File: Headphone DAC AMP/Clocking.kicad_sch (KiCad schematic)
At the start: 13 parts, among them Y1 Crystal_GND24, Y2 LMK6CE049152CDLFR, Y3 ASDLJ-E-45.1584MHz

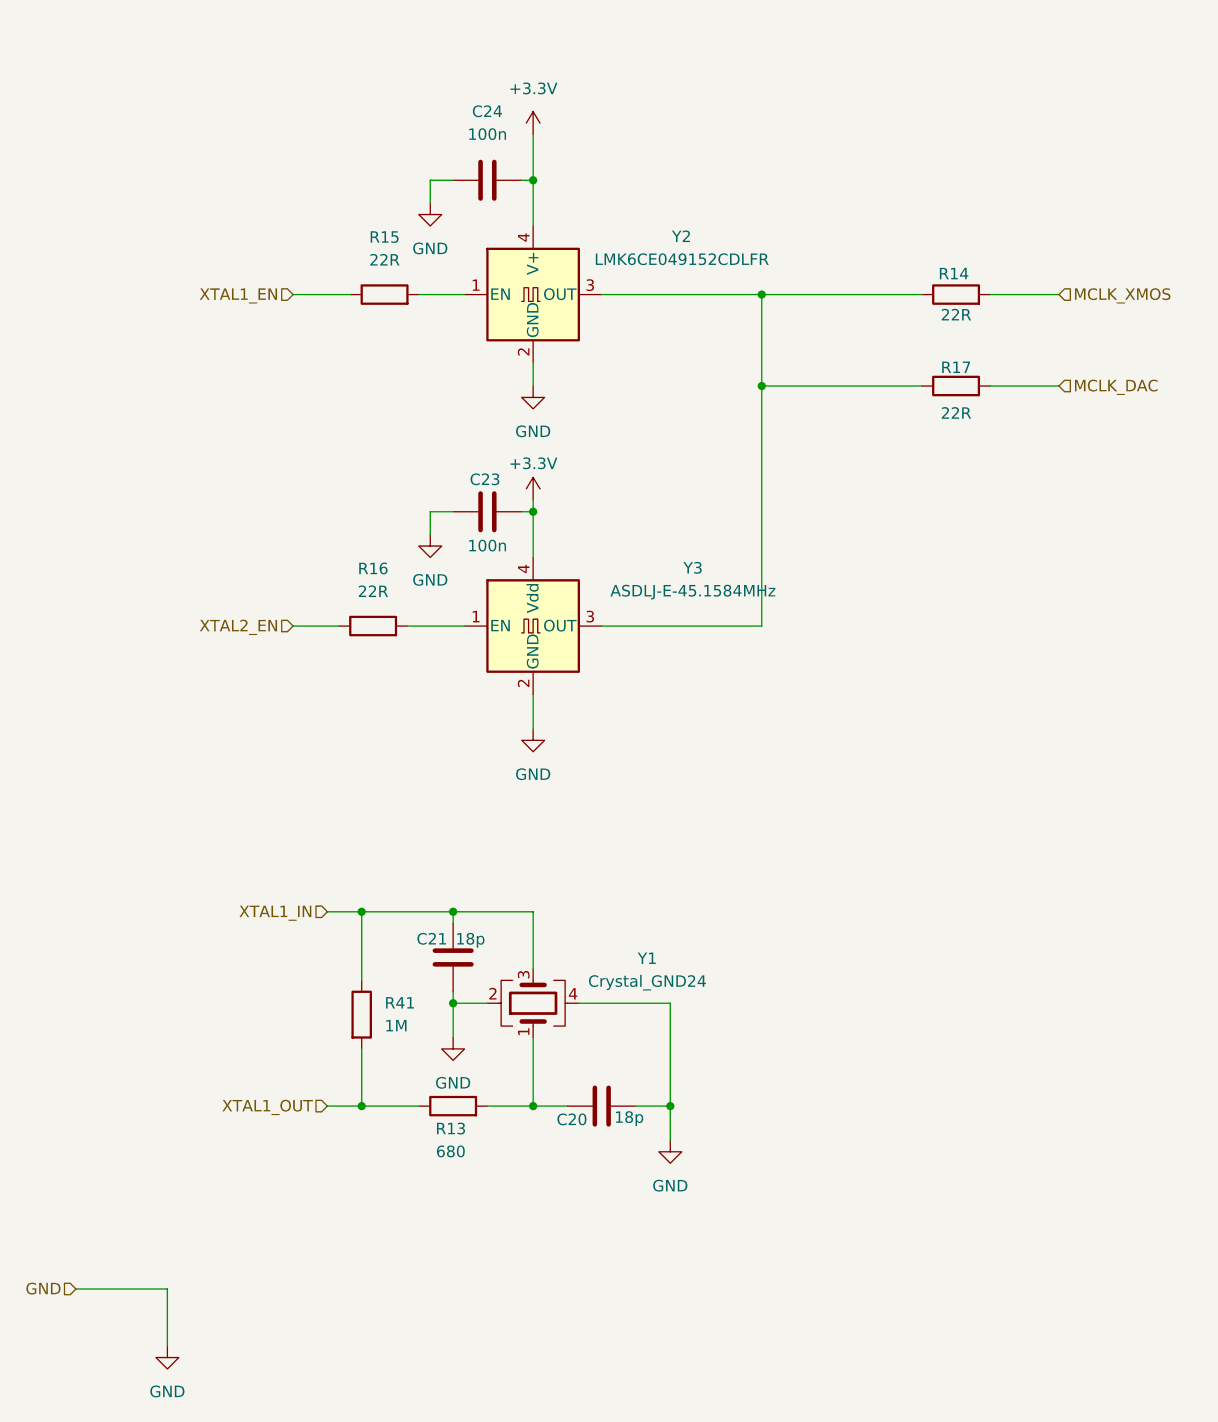
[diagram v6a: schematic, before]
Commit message: Cleaned Up and Annotated Schematic
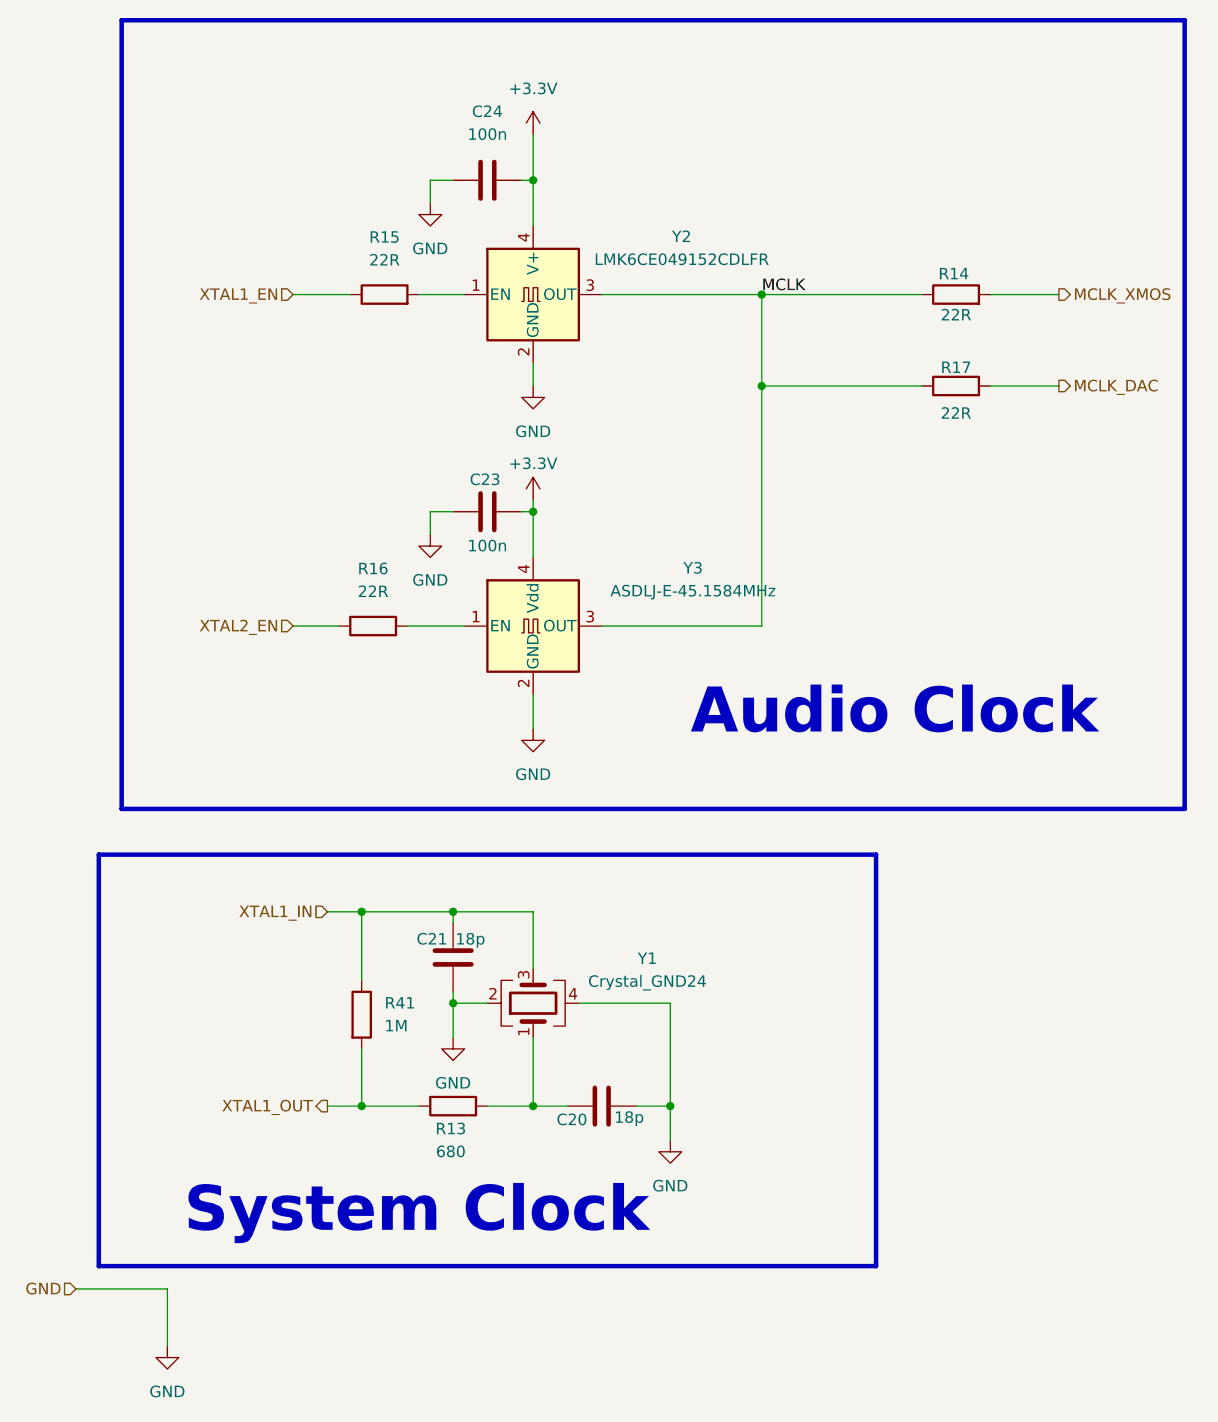
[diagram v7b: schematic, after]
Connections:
- net MCLK: now reaches R14.1, R17.1, Y2.3 (OUT), Y3.3 (OUT)
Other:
- note added: "Audio Clock"
- note added: "System Clock"
- company: (none) -> Personal Project - Kettering University
- title: (none) -> Hi-Fidelity USB DAC Amplifier
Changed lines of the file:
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@@
 	(generator_version "9.0")
 	(paper "A4")
+	(title_block
+		(title "Hi-Fidelity USB DAC Amplifier")
+		(date "2025-11-19")
+		(rev "1.0")
+		(company "Personal Project - Kettering University")
+		(comment 1 "Designed by Dan Abidov & Luke Stirzinger")
+		(comment 2 "Based on XMOS Xu316 and ES9039Q2M")
+	)
+	(rectangle
+		(start 49.53 110.49)
+		(end 135.89 156.21)
+		(stroke
+			(width 0.5)
+			(type default)
+			(color 194 0 0 1)
+		)
+		(fill
+			(type none)
+		)
+	)
+	(rectangle
+		(start 52.07 17.78)
+		(end 170.18 105.41)
+		(stroke
+			(width 0.5)
+			(type default)
+			(color 194 0 0 1)
+		)
+		(fill
+			(type none)
+		)
+	)
+	(text "System Clock"
+		(exclude_from_sim no)
+		(at 84.836 150.114 0)
+		(effects
+			(font
+				(size 5 5)
+				(thickness 1)
+				(bold yes)
+				(color 132 0 132 1)
+			)
+		)
+	)
+	(text "Audio Clock"
+		(exclude_from_sim no)
+		(at 137.922 94.742 0)
+		(effects
+			(font
+				(size 5 5)
+				(thickness 1)
+				(bold yes)
+				(color 132 0 132 1)
+			)
+		)
+	)
 	(junction
 		(at 97.79 35.56)
@@
 		)
 	)
+	(label "MCLK"
+		(at 123.19 48.26 0)
+		(effects
+			(font
+				(size 1.27 1.27)
+			)
+			(justify left bottom)
+		)
+	)
 	(hierarchical_label "MCLK_XMOS"
-		(shape input)
+		(shape output)
 		(at 156.21 48.26 0)
 		(effects
@@
 	)
 	(hierarchical_label "XTAL1_OUT"
-		(shape input)
+		(shape output)
 		(at 74.93 138.43 180)
 		(effects
@@
 	)
 	(hierarchical_label "MCLK_DAC"
-		(shape input)
+		(shape output)
 		(at 156.21 58.42 0)
 		(effects

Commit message: Schematic V1 Done
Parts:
- R41: footprint Inductor_SMD:L_0805_2012Metric -> Resistor_SMD:R_0805_2012Metric_Pad1.20x1.40mm_HandSolder
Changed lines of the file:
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@@
 			)
 		)
-		(property "Footprint" "Inductor_SMD:L_0805_2012Metric"
+		(property "Footprint" "Resistor_SMD:R_0805_2012Metric_Pad1.20x1.40mm_HandSolder"
 			(at 76.962 128.27 90)
 			(effects
